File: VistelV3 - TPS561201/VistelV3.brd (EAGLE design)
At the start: 130 x 140 mm, 189 parts, among them IC1 LD117ADT33TR, IC5 SI7006-A10-IM, J2 RJ45-ABRACON-11108B, J3 RJ45-ABRACON-11108B, K1 ZF112, K2 ZF112, K3 ZF112, K4 ZF112, T1 MOSFET-NCHANNELBSS123LT1G, T2 MOSFET-NCHANNELBSS123LT1G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

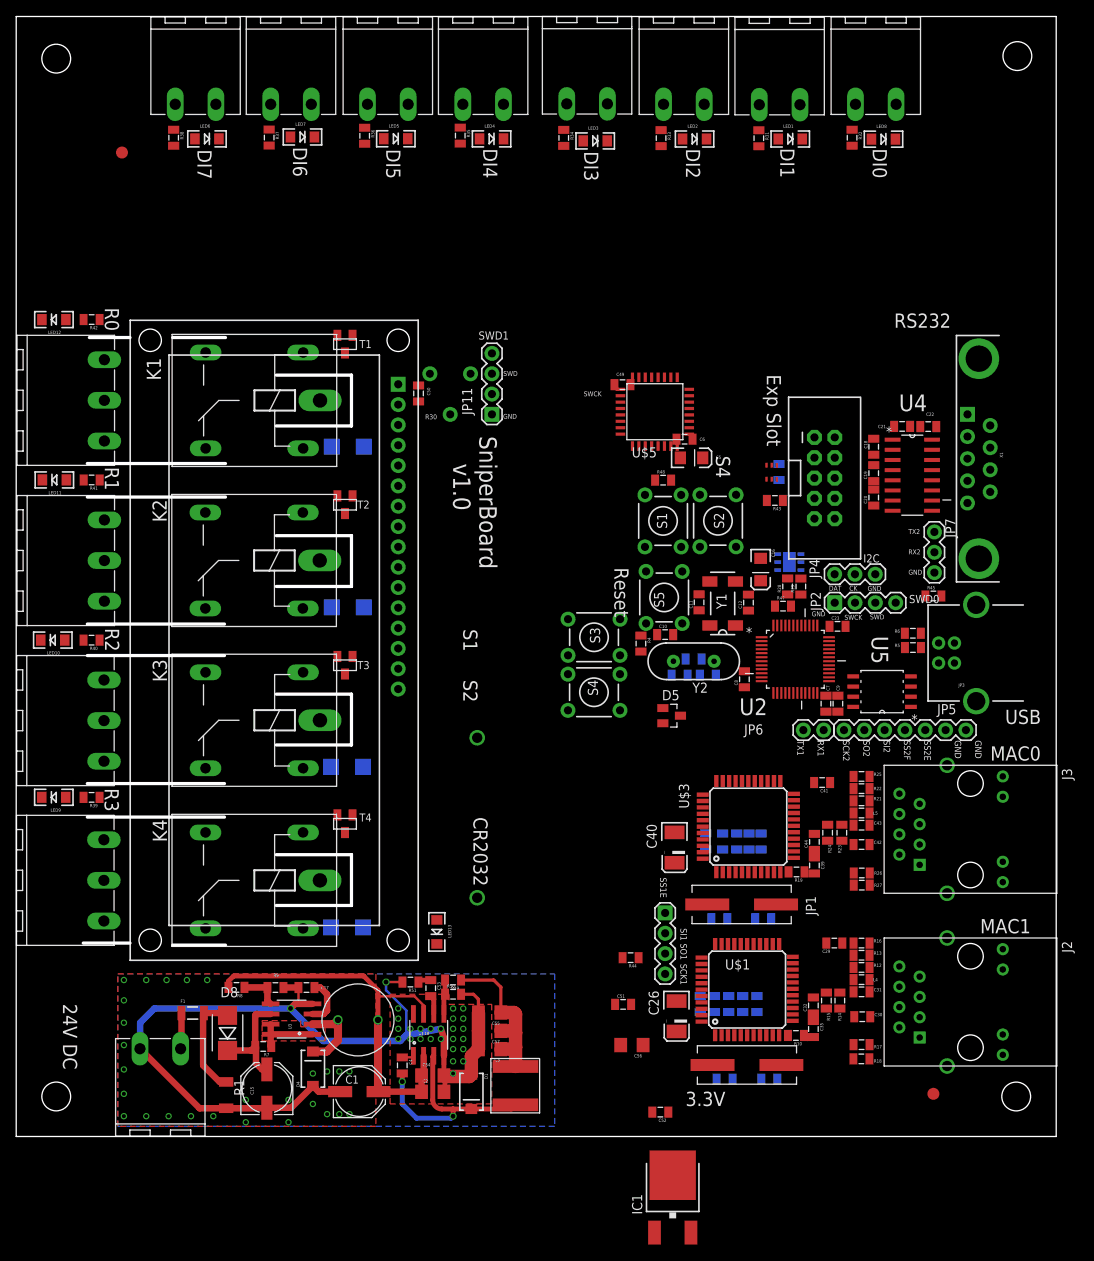
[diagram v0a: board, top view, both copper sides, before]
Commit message: Updated Power suply section
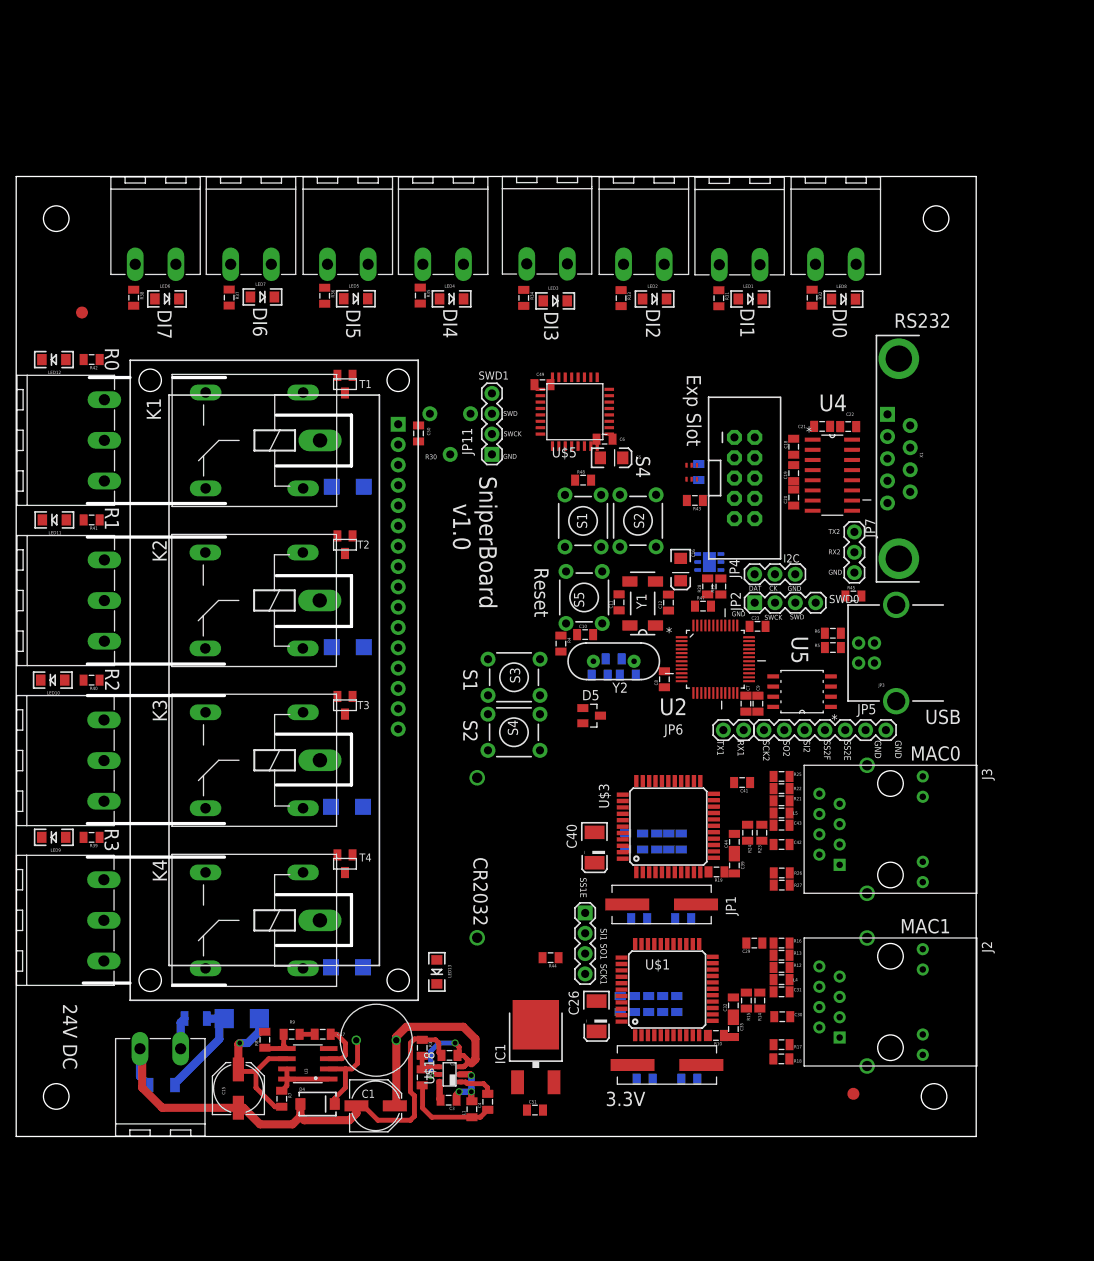
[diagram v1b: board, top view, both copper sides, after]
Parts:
- removed C52: 0.1uF, SparkFun-Passives:0805
- removed C53: 1.5nF, SparkFun-Passives:0805
- removed C54, C55, C56, C57: 10uF CC1206ZKY5V7BB106, SparkFun-Passives:1206
- removed D1: (no value), SparkFun-DiscreteSemi:SMA-DIODE
- removed R49: 15.5K, SparkFun-Passives:0805
- removed R50: 10K, SparkFun-Passives:0805
- removed R51: 12K, SparkFun-Passives:0805
- added R2: 41.2K, SparkFun-Passives:0805
- added R3: 10K, SparkFun-Passives:0805
- C2, C3: value 10uF CC1206ZKY5V7BB106 -> 0.1uF; device SparkFun-Passives:1206 -> SparkFun-Passives:0805
- C4: value 10nF -> 22uF 6.3V JMK212BJ476MG
- L1: value 22uH NR6045T220M -> 4.7uH SRN6045-4R7Y; device SparkFun-Passives:NR6045-IND -> SparkFun-Passives:0805
- U$18: value ACT4060A -> (none); device VistelV3:SO08 -> VistelV3:TSOT23-6_DDC
- moved IC1 25.4 mm to (65.0, 11.6)
- moved U$10 20.6 mm to (17.4, 109.0)
- moved U$11 20.6 mm to (29.4, 109.0)
- moved U$12 20.6 mm to (53.4, 109.0)
- moved U$13 20.6 mm to (78.5, 109.0)
- moved U$6 20.6 mm to (102.5, 109.0)
- moved U$9 20.6 mm to (41.5, 109.0)
- moved FID2 20.6 mm to (8.22, 103.0)
- moved LED1 20.6 mm to (91.8, 104.7)
- moved LED2 20.6 mm to (79.8, 104.7)
- moved LED3 20.6 mm to (67.4, 104.4)
- moved LED4 20.6 mm to (54.4, 104.7)
- moved LED5 20.6 mm to (42.5, 104.7)
- moved LED6 20.6 mm to (18.8, 104.7)
- moved LED7 20.6 mm to (30.8, 104.9)
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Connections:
- removed net N$18: C4.2, D1.C, L1.P$1, U$18.3
- removed net N$23: C53.2, U$18.6
- removed net N$32: C53.1, R51.1
- new net N$20: IC1.3, R2.1, R3.2, U$18.4
- net +12V: now also U$18.3, U$18.5; no longer C54.1, U$18.2, U$18.7
- net +5V: now also C4.1, L1.1, R2.2; no longer C3.1, C52.1, C55.1, C57.1, IC1.3, L1.P$2, R49.1
- net 3.3V: no longer C56.1
- net GND: now also C4.2, R3.1, U$18.1; no longer C3.2, C52.2, C54.2, C55.2, C56.2, C57.2, D1.A, R50.2, R51.2, U$18.4
- net N$19: now also C3.2, U$18.6; no longer R49.2, R50.1, U$18.5
- net N$6: now also C3.1, L1.2, U$18.2; no longer C4.1, U$18.1
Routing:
- net GND: track 113.7 -> 71.8 mm, vias 52 -> 0
- net N$18: track 28.5 -> 0.00 mm, vias 2 -> 0
- net +12V: track 50.5 -> 36.1 mm, vias 0 -> 2
- net +5V: track 20.9 -> 11.9 mm
- net VIN: track 13.4 -> 21.1 mm, vias 0 -> 1
- net N$6: track 1.48 -> 7.48 mm, vias 0 -> 3
- net N$20: track 0.00 -> 4.00 mm
- net N$23: track 2.38 -> 0.00 mm
- net N$24: track 9.67 -> 11.8 mm
- net N$19: track 4.30 -> 2.33 mm
- net N$32: track 1.64 -> 0.00 mm
- net N$5: track 13.5 -> 12.8 mm
- net N$4: track 4.57 -> 3.97 mm
- net N$2: track 0.51 -> 0.00 mm
- removed copper zone on layer 1, net GND
- removed copper zone on layer 16, net GND
- removed copper zone on layer 1, net VIN2
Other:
- board size 130 x 140 mm -> 120 x 120 mm
